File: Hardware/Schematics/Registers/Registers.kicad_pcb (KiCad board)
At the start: 2 copper layers, 19 parts, among them J1 Conn_01x19, J2 Conn_01x08, J3 Conn_01x08, U1 74LS139, U10 74LS245, U11 74LS245, U12 74LS245, U13 74LS245, U14 74LS245, U15 74LS245, U16 74LS245, U2 74LS139, U3 74LS377, U4 74LS377, U5 74LS377, U6 74LS377, U7 74LS377, U8 74LS377, U9 74LS245

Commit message: Interim
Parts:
- removed U4, U6: 74LS377, Package_DIP:DIP-20_W7.62mm_LongPads
- added A0: LED, LED_THT:LED_D3.0mm, F.Cu at (17.0, 77.1)
- added A1: LED, LED_THT:LED_D3.0mm, F.Cu at (17.0, 82.0)
- added A2: LED, LED_THT:LED_D3.0mm, F.Cu at (17.0, 87.0)
- added A3: LED, LED_THT:LED_D3.0mm, F.Cu at (17.0, 91.9)
- added A4: LED, LED_THT:LED_D3.0mm, F.Cu at (17.0, 96.7)
- added A5: LED, LED_THT:LED_D3.0mm, F.Cu at (17.0, 101.6)
- added A6: LED, LED_THT:LED_D3.0mm, F.Cu at (17.0, 106.5)
- added A7: LED, LED_THT:LED_D3.0mm, F.Cu at (17.0, 111.4)
- added B0: LED, LED_THT:LED_D3.0mm, F.Cu at (25.5, 77.1)
- added B1: LED, LED_THT:LED_D3.0mm, F.Cu at (25.5, 82.0)
- added B2: LED, LED_THT:LED_D3.0mm, F.Cu at (25.5, 86.9)
- added B3: LED, LED_THT:LED_D3.0mm, F.Cu at (25.5, 91.9)
- added B4: LED, LED_THT:LED_D3.0mm, F.Cu at (25.5, 96.7)
- added B5: LED, LED_THT:LED_D3.0mm, F.Cu at (25.5, 101.6)
- added B6: LED, LED_THT:LED_D3.0mm, F.Cu at (25.4, 106.5)
- added B7: LED, LED_THT:LED_D3.0mm, F.Cu at (25.4, 111.4)
- added D10: LED, LED_THT:LED_D3.0mm, F.Cu at (96.3, 128.5)
- added D12: LED, LED_THT:LED_D3.0mm, F.Cu at (131.5, 134.9)
- added D14: LED, LED_THT:LED_D3.0mm, F.Cu at (94.0, 143.6)
- added D15: LED, LED_THT:LED_D3.0mm, F.Cu at (79.0, 151.1)
- added D16: LED, LED_THT:LED_D3.0mm, F.Cu at (79.0, 129.6)
- added D25: LED, LED_THT:LED_D3.0mm, F.Cu at (113.6, 119.8)
- added D26: LED, LED_THT:LED_D3.0mm, F.Cu at (116.5, 142.4)
- added D27: LED, LED_THT:LED_D3.0mm, F.Cu at (128.6, 112.2)
- added D28: LED, LED_THT:LED_D3.0mm, F.Cu at (33.6, 77.2)
- added D29: LED, LED_THT:LED_D3.0mm, F.Cu at (94.0, 136.0)
- added D30: LED, LED_THT:LED_D3.0mm, F.Cu at (33.6, 82.1)
- added D31: LED, LED_THT:LED_D3.0mm, F.Cu at (101.5, 136.0)
- added D32: LED, LED_THT:LED_D3.0mm, F.Cu at (26.9, 138.9)
- added D33: LED, LED_THT:LED_D3.0mm, F.Cu at (126.3, 127.3)
- added D34: LED, LED_THT:LED_D3.0mm, F.Cu at (32.7, 138.2)
- added D35: LED, LED_THT:LED_D3.0mm, F.Cu at (124.0, 142.4)
- added D36: LED, LED_THT:LED_D3.0mm, F.Cu at (38.8, 137.4)
- added D37: LED, LED_THT:LED_D3.0mm, F.Cu at (143.6, 119.8)
- added D38: LED, LED_THT:LED_D3.0mm, F.Cu at (44.8, 137.4)
- added D39: LED, LED_THT:LED_D3.0mm, F.Cu at (51.7, 136.5)
- added D4: LED, LED_THT:LED_D3.0mm, F.Cu at (79.0, 143.6)
- added D40: LED, LED_THT:LED_D3.0mm, F.Cu at (58.4, 136.3)
- added D41: LED, LED_THT:LED_D3.0mm, F.Cu at (86.5, 151.1)
- added D42: LED, LED_THT:LED_D3.0mm, F.Cu at (111.3, 127.3)
- added D43: LED, LED_THT:LED_D3.0mm, F.Cu at (71.5, 129.6)
- added D44: LED, LED_THT:LED_D3.0mm, F.Cu at (116.5, 134.9)
- added D45: LED, LED_THT:LED_D3.0mm, F.Cu at (109.0, 136.0)
- added D46: LED, LED_THT:LED_D3.0mm, F.Cu at (109.0, 143.6)
- added D47: LED, LED_THT:LED_D3.0mm, F.Cu at (121.1, 112.2)
- added D48: LED, LED_THT:LED_D3.0mm, F.Cu at (64.0, 144.7)
- added D6: LED, LED_THT:LED_D3.0mm, F.Cu at (124.0, 134.9)
- added D8: LED, LED_THT:LED_D3.0mm, F.Cu at (113.6, 112.2)
- added RD1: 74LS377, Package_DIP:DIP-20_W7.62mm_LongPads, F.Cu at (56.4, 73.6)
- added RN1: R_Network08, Resistor_THT:R_Array_SIP9, F.Cu at (63.7, 119.3)
- added RN2: R_Network08, Resistor_THT:R_Array_SIP9, F.Cu at (88.5, 115.0)
- added RN3: R_Network08, Resistor_THT:R_Array_SIP9, F.Cu at (63.7, 123.7)
- added RN4: R_Network08, Resistor_THT:R_Array_SIP9, F.Cu at (63.7, 110.6)
- added RN5: R_Network08, Resistor_THT:R_Array_SIP9, F.Cu at (88.5, 110.6)
- added RN6: R_Network08, Resistor_THT:R_Array_SIP9, F.Cu at (63.7, 115.0)
- added RS1: 74LS377, Package_DIP:DIP-20_W7.62mm_LongPads, F.Cu at (86.1, 73.4)
- moved U1 123.1 mm to (132.3, 28.2)
- moved U2 122.9 mm to (132.4, 51.6)
- moved U16 118.2 mm to (115.8, 29.0), turned to 0 degrees
- moved U8 112.3 mm to (87.1, 22.2)
- moved U15 104.4 mm to (103.0, 29.0), turned to 0 degrees
- moved U14 90.7 mm to (90.1, 29.0), turned to 0 degrees
- moved U13 76.9 mm to (77.3, 29.0), turned to 0 degrees
- moved J2 66.8 mm to (59.2, 80.4), turned to 90 degrees
- moved U12 63.2 mm to (64.4, 29.0), turned to 0 degrees
- moved U11 49.6 mm to (51.6, 29.0), turned to 0 degrees
- moved U10 36.1 mm to (38.7, 29.0), turned to 0 degrees
- moved U5 35.4 mm to (57.3, 22.2)
- moved J3 27.6 mm to (88.5, 80.4), turned to 90 degrees
- moved U7 26.7 mm to (116.8, 22.2)
- moved U9 22.9 mm to (25.9, 29.3), turned to 0 degrees
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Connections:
- U10 pad 1: unconnected-(U10-Pad1) -> VCC
- U11 pad 1: unconnected-(U11-Pad1) -> VCC
- U12 pad 1: unconnected-(U12-Pad1) -> VCC
- U13 pad 1: unconnected-(U13-Pad1) -> VCC
- U14 pad 1: unconnected-(U14-Pad1) -> VCC
- U15 pad 1: unconnected-(U15-Pad1) -> VCC
- U16 pad 1: unconnected-(U16-Pad1) -> VCC
- U5 pad 15: unconnected-(U5-Pad15) -> Net-(U5-Pad15)
- U8 pad 19: unconnected-(U8-Pad19) -> Net-(U8-Pad19)
- U9 pad 1: unconnected-(U9-Pad1) -> VCC
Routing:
- net VCC: track 449.2 -> 0.00 mm
- net GND: track 432.7 -> 0.00 mm
- net Net-(J1-Pad6): track 97.1 -> 0.00 mm, vias 1 -> 0
- net Net-(J1-Pad5): track 94.5 -> 0.00 mm
- net Net-(J1-Pad4): track 87.3 -> 0.00 mm
- net Net-(J1-Pad9): track 79.5 -> 0.00 mm
- net Net-(J1-Pad8): track 65.4 -> 0.00 mm
- net Net-(J1-Pad7): track 54.4 -> 0.00 mm

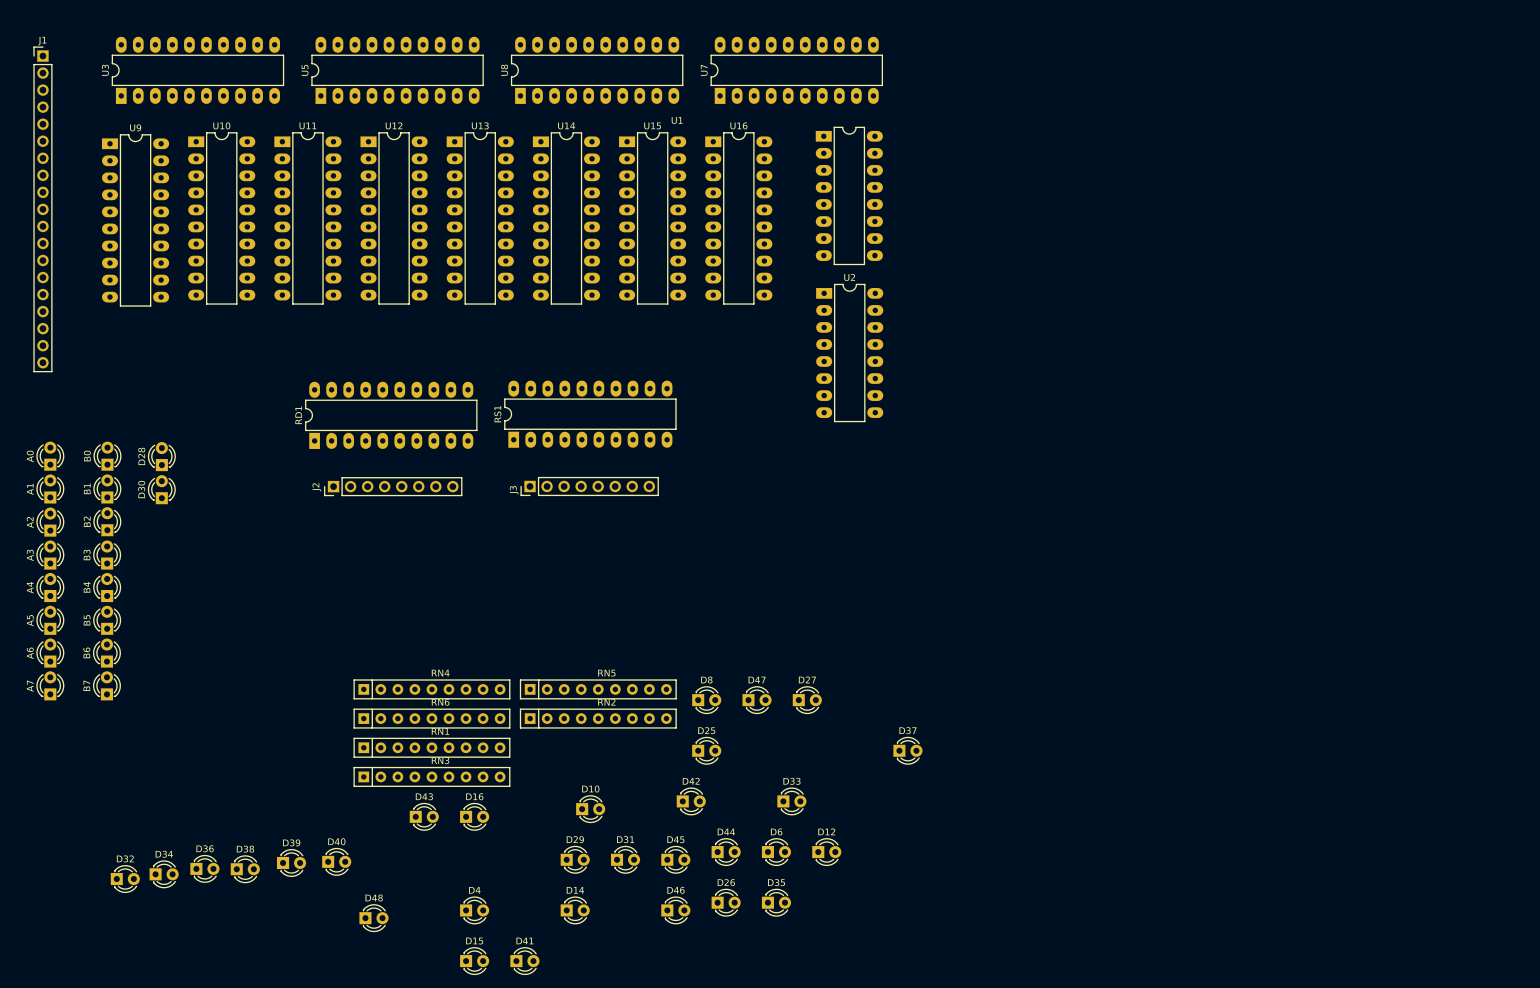
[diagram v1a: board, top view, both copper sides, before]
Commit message: Finished Datapath Controller
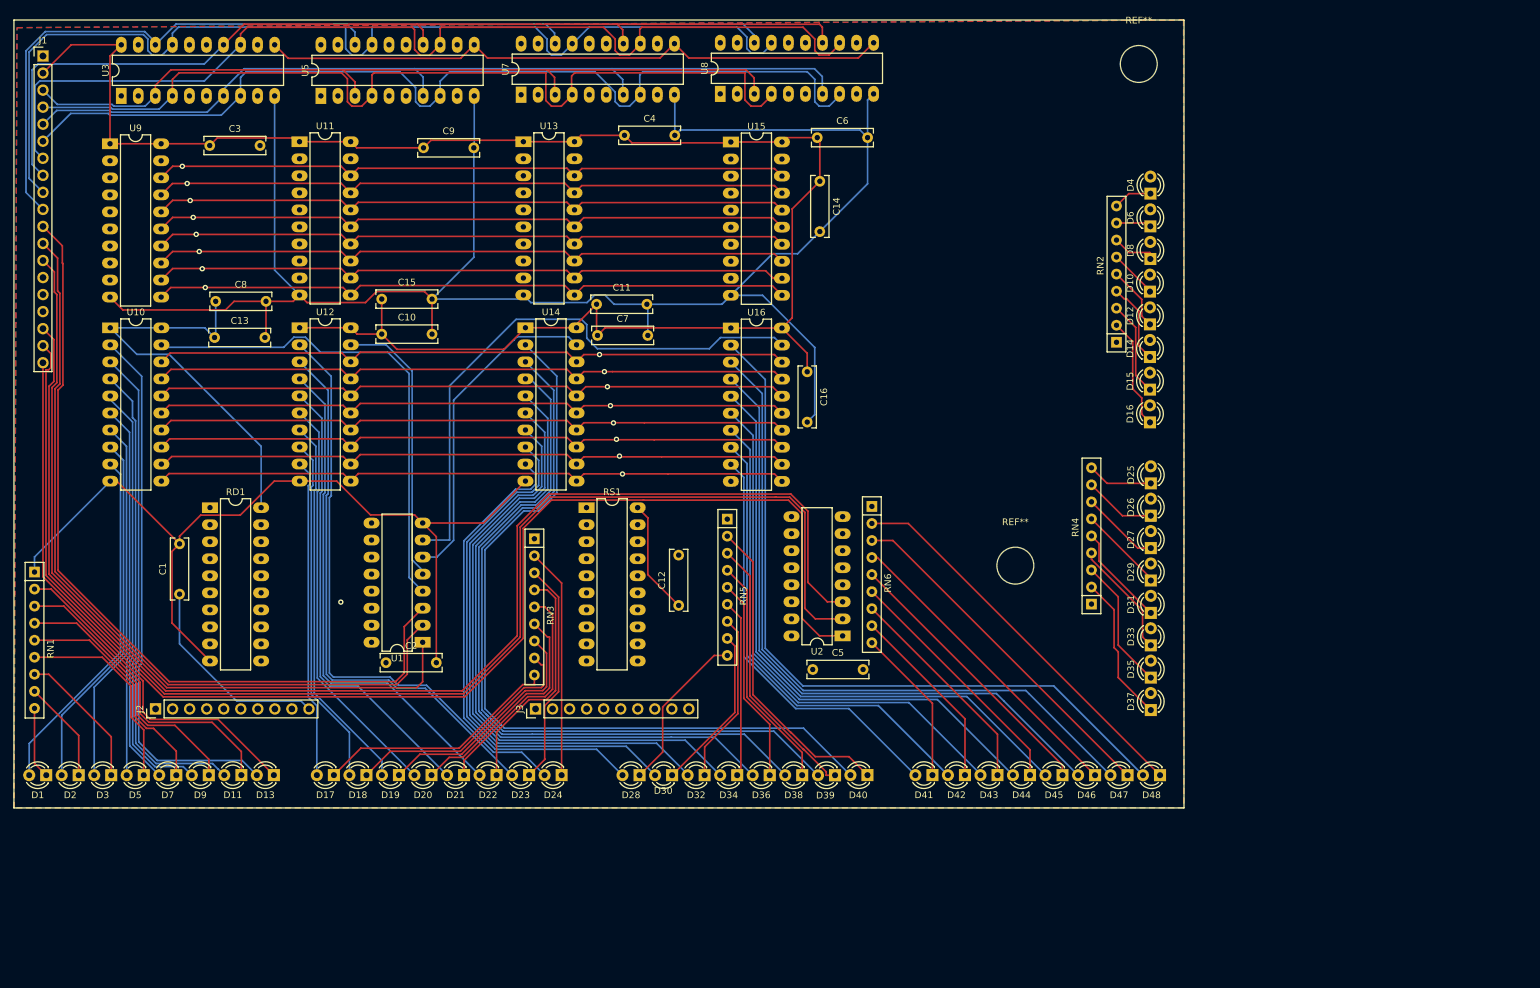
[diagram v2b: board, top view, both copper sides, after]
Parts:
- added C1: C, Capacitor_THT:C_Rect_L9.0mm_W2.5mm_P7.50mm_MKT, F.Cu at (36.3, 96.4)
- added C10: C, Capacitor_THT:C_Rect_L9.0mm_W2.5mm_P7.50mm_MKT, F.Cu at (66.4, 57.7)
- added C11: C, Capacitor_THT:C_Rect_L9.0mm_W2.5mm_P7.50mm_MKT, F.Cu at (98.4, 53.2)
- added C12: C, Capacitor_THT:C_Rect_L9.0mm_W2.5mm_P7.50mm_MKT, F.Cu at (110.7, 98.1)
- added C13: C, Capacitor_THT:C_Rect_L9.0mm_W2.5mm_P7.50mm_MKT, F.Cu at (41.5, 58.2)
- added C14: C, Capacitor_THT:C_Rect_L9.0mm_W2.5mm_P7.50mm_MKT, F.Cu at (131.7, 34.9)
- added C15: C, Capacitor_THT:C_Rect_L9.0mm_W2.5mm_P7.50mm_MKT, F.Cu at (66.4, 52.5)
- added C16: C, Capacitor_THT:C_Rect_L9.0mm_W2.5mm_P7.50mm_MKT, F.Cu at (129.8, 63.3)
- added C2: C, Capacitor_THT:C_Rect_L9.0mm_W2.5mm_P7.50mm_MKT, F.Cu at (67.0, 106.7)
- added C3: C, Capacitor_THT:C_Rect_L9.0mm_W2.5mm_P7.50mm_MKT, F.Cu at (40.8, 29.6)
- added C4: C, Capacitor_THT:C_Rect_L9.0mm_W2.5mm_P7.50mm_MKT, F.Cu at (102.6, 28.0)
- added C5: C, Capacitor_THT:C_Rect_L9.0mm_W2.5mm_P7.50mm_MKT, F.Cu at (130.7, 107.7)
- added C6: C, Capacitor_THT:C_Rect_L9.0mm_W2.5mm_P7.50mm_MKT, F.Cu at (131.3, 28.4)
- added C7: C, Capacitor_THT:C_Rect_L9.0mm_W2.5mm_P7.50mm_MKT, F.Cu at (98.6, 57.9)
- added C8: C, Capacitor_THT:C_Rect_L9.0mm_W2.5mm_P7.50mm_MKT, F.Cu at (41.6, 52.8)
- added C9: C, Capacitor_THT:C_Rect_L9.0mm_W2.5mm_P7.50mm_MKT, F.Cu at (72.6, 29.9)
- added REF**: MountingHole_5.5mm, MountingHole:MountingHole_5.5mm, F.Cu at (179.3, 17.4)
- added REF**: MountingHole_5.5mm, MountingHole:MountingHole_5.5mm, F.Cu at (160.9, 92.2)
- J2, J3: footprint Connector_PinHeader_2.54mm:PinHeader_1x08_P2.54mm_Vertical -> Connector_PinHeader_2.54mm:PinHeader_1x10_P2.54mm_Vertical
- moved D4 147.7 mm to (181.0, 36.7), turned to 90 degrees
- moved D15 132.9 mm to (180.9, 66.0), turned to 90 degrees
- moved D48 120.4 mm to (182.4, 123.4), turned to 180 degrees
- moved D14 119.9 mm to (180.9, 61.1), turned to 90 degrees
- moved D16 117.7 mm to (180.9, 70.8), turned to 90 degrees
- moved D10 114.5 mm to (180.9, 51.3), turned to 90 degrees
- moved D6 109.3 mm to (181.0, 41.6), turned to 90 degrees
- moved RN4 109.2 mm to (172.2, 97.9), turned to 90 degrees
- moved RN2 103.9 mm to (175.9, 58.9), turned to 90 degrees
- moved D29 96.5 mm to (181.1, 94.4), turned to 90 degrees
- moved U1 96.3 mm to (72.5, 103.6), turned to 180 degrees
- moved D8 94.2 mm to (181.0, 46.5), turned to 90 degrees
- moved D12 92.9 mm to (180.9, 56.2), turned to 90 degrees
- moved D32 89.0 mm to (114.5, 123.4), turned to 180 degrees
- moved D34 88.0 mm to (119.4, 123.4), turned to 180 degrees
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- renumbered A7 to D1, A1 to D11, A0 to D13, B0 to D17, B1 to D18, B2 to D19, A6 to D2, B3 to D20, B4 to D21, B5 to D22, B6 to D23, B7 to D24, A5 to D3, A4 to D5, A3 to D7, A2 to D9
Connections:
- D10 pad 2: Net-(J2-Pad5) -> Net-(D10-Pad2)
- D12 pad 2: Net-(J2-Pad4) -> Net-(D12-Pad2)
- D14 pad 2: Net-(J2-Pad3) -> Net-(D14-Pad2)
- D15 pad 2: Net-(J2-Pad2) -> Net-(D15-Pad2)
- D16 pad 2: Net-(J2-Pad1) -> Net-(D16-Pad2)
- D19 pad 2: Net-(U5-Pad15) -> Net-(U12-Pad7)
- D25 pad 2: Net-(J3-Pad8) -> Net-(D25-Pad2)
- D26 pad 2: Net-(J3-Pad7) -> Net-(D26-Pad2)
- D27 pad 2: Net-(J3-Pad6) -> Net-(D27-Pad2)
- D29 pad 2: Net-(J3-Pad5) -> Net-(D29-Pad2)
- D31 pad 2: Net-(J3-Pad4) -> Net-(D31-Pad2)
- D33 pad 2: Net-(J3-Pad3) -> Net-(D33-Pad2)
- D35 pad 2: Net-(J3-Pad2) -> Net-(D35-Pad2)
- D37 pad 2: Net-(J3-Pad1) -> Net-(D37-Pad2)
- D4 pad 2: Net-(J2-Pad8) -> Net-(D4-Pad2)
- D41 pad 2: Net-(U8-Pad19) -> Net-(D41-Pad2)
- D6 pad 2: Net-(J2-Pad7) -> Net-(D6-Pad2)
- D8 pad 2: Net-(J2-Pad6) -> Net-(D8-Pad2)
- J1 pad 10: unconnected-(J1-Pad10) -> Net-(U3-Pad18)
- J1 pad 3: unconnected-(J1-Pad3) -> Net-(U3-Pad3)
- J2 pad 1: Net-(J2-Pad1) -> GND
- J2 pad 2: Net-(J2-Pad2) -> Net-(D16-Pad2)
- J2 pad 3: Net-(J2-Pad3) -> Net-(D15-Pad2)
- J2 pad 4: Net-(J2-Pad4) -> Net-(D14-Pad2)
- J2 pad 5: Net-(J2-Pad5) -> Net-(D12-Pad2)
- J2 pad 6: Net-(J2-Pad6) -> Net-(D10-Pad2)
- J2 pad 7: Net-(J2-Pad7) -> Net-(D8-Pad2)
- J2 pad 8: Net-(J2-Pad8) -> Net-(D6-Pad2)
- J3 pad 1: Net-(J3-Pad1) -> GND
- J3 pad 2: Net-(J3-Pad2) -> Net-(D37-Pad2)
- J3 pad 3: Net-(J3-Pad3) -> Net-(D35-Pad2)
- J3 pad 4: Net-(J3-Pad4) -> Net-(D33-Pad2)
- J3 pad 5: Net-(J3-Pad5) -> Net-(D31-Pad2)
- J3 pad 6: Net-(J3-Pad6) -> Net-(D29-Pad2)
- J3 pad 7: Net-(J3-Pad7) -> Net-(D27-Pad2)
- J3 pad 8: Net-(J3-Pad8) -> Net-(D26-Pad2)
- RD1 pad 12: Net-(J2-Pad5) -> Net-(D10-Pad2)
- RD1 pad 14: Net-(U11-Pad13) -> Net-(RD1-Pad14)
- RD1 pad 15: Net-(J2-Pad6) -> Net-(D8-Pad2)
- RD1 pad 16: Net-(J2-Pad7) -> Net-(D6-Pad2)
- RD1 pad 19: Net-(J2-Pad8) -> Net-(D4-Pad2)
- RD1 pad 2: Net-(J2-Pad1) -> Net-(D16-Pad2)
- RD1 pad 5: Net-(J2-Pad2) -> Net-(D15-Pad2)
- RD1 pad 6: Net-(J2-Pad3) -> Net-(D14-Pad2)
- RD1 pad 9: Net-(J2-Pad4) -> Net-(D12-Pad2)
- RS1 pad 12: Net-(J3-Pad5) -> Net-(D29-Pad2)
- RS1 pad 15: Net-(J3-Pad6) -> Net-(D27-Pad2)
- RS1 pad 16: Net-(J3-Pad7) -> Net-(D26-Pad2)
- RS1 pad 19: Net-(J3-Pad8) -> Net-(D25-Pad2)
- RS1 pad 2: Net-(J3-Pad1) -> Net-(D37-Pad2)
- RS1 pad 5: Net-(J3-Pad2) -> Net-(D35-Pad2)
- RS1 pad 6: Net-(J3-Pad3) -> Net-(D33-Pad2)
- RS1 pad 9: Net-(J3-Pad4) -> Net-(D31-Pad2)
- U11 pad 13: Net-(U11-Pad13) -> Net-(RD1-Pad14)
- U11 pad 7: Net-(U11-Pad7) -> Net-(U12-Pad7)
- U12 pad 7: Net-(U11-Pad7) -> Net-(U12-Pad7)
- U13 pad 13: Net-(U11-Pad13) -> Net-(RD1-Pad14)
- U15 pad 13: unconnected-(U15-Pad13) -> Net-(RD1-Pad14)
- U15 pad 9: Net-(U15-Pad9) -> Net-(D41-Pad2)
- U16 pad 9: Net-(U15-Pad9) -> Net-(D41-Pad2)
- U5 pad 15: Net-(U5-Pad15) -> Net-(U12-Pad7)
- U8 pad 19: Net-(U8-Pad19) -> Net-(D41-Pad2)
- U9 pad 13: Net-(U11-Pad13) -> Net-(RD1-Pad14)
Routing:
- net GND: track 0.00 -> 689.1 mm
- net VCC: track 0.00 -> 539.5 mm
- net Net-(D4-Pad2): track 0.00 -> 235.7 mm
- net Net-(D16-Pad2): track 0.00 -> 226.8 mm
- net Net-(D6-Pad2): track 0.00 -> 224.4 mm
- net Net-(D8-Pad2): track 0.00 -> 220.7 mm
- net Net-(D15-Pad2): track 0.00 -> 216.9 mm
- net Net-(D14-Pad2): track 0.00 -> 215.8 mm
- net Net-(D10-Pad2): track 0.00 -> 213.6 mm
- net Net-(D12-Pad2): track 0.00 -> 211.2 mm
- net Net-(J1-Pad18): track 0.00 -> 199.0 mm
- net Net-(J1-Pad19): track 0.00 -> 197.8 mm
- net Net-(J1-Pad17): track 0.00 -> 197.7 mm
- net Net-(D34-Pad2): track 0.00 -> 174.5 mm
- net Net-(D39-Pad2): track 0.00 -> 166.5 mm
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- added copper zone on B.Cu, net GND
- added copper zone on F.Cu, net GND
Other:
- copper layers 2 -> 4
